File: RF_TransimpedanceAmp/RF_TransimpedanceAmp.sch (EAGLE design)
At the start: 11 parts, among them IC1 OPA847, IC3 PMA-5452, X1 UMC

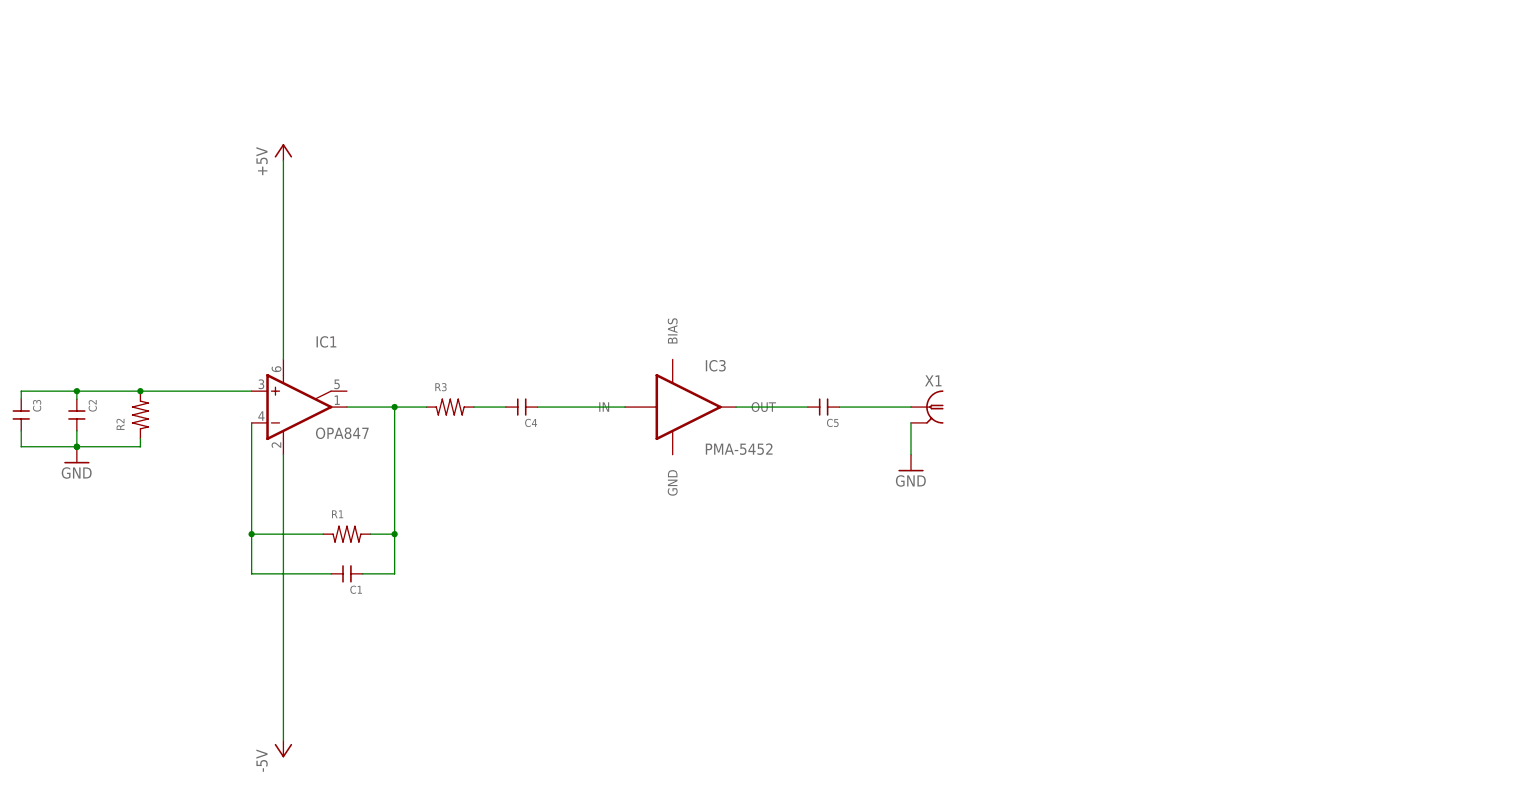
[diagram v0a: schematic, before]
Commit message: Schematic done; routing in progress. Want to check with alessandro.
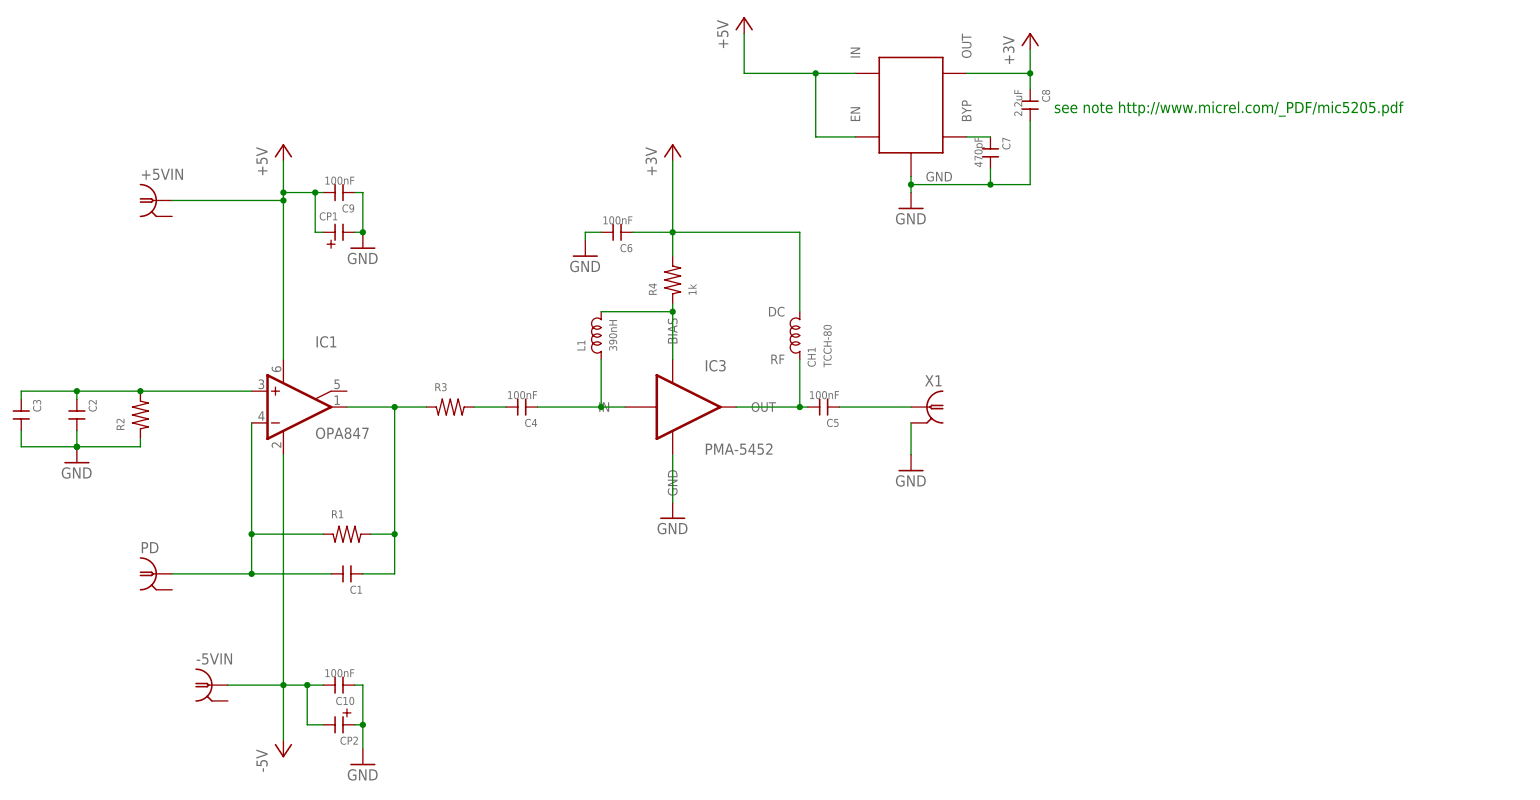
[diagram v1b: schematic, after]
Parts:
- added +5VIN, -5VIN: UMC, connector-jqi:UMC
- added C10, C6, C9: 100nF, rlc-jqi:CAP0201
- added C7: 470pF, rlc-jqi:CAP0201
- added C8: 2.2uF, rlc-jqi:CAP0402
- added CH1: TCCH-80, rf-jqi:TCCH-80
- added CP1, CP2: (no value), rlc-jqi:CAP-POL0603
- added L1: 390nH, rlc-jqi:INDUCTOR-0402
- added PD: SMA, connector-jqi:SMA
- added R4: 1k, rlc-jqi:RES0402
- added U$1: MIC5205, regulator-jqi:MIC5205
- C4, C5: value (none) -> 100nF
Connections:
- new net +3V: C6.P$1, C8.P$1, CH1.DC, R4.P$2, U$1.OUT
- new net N$10: C7.P$1, U$1.BYP
- new net N$9: IC3.BIAS, L1.P$2, R4.P$1
- net +5V: now also +5VIN.1, C9.P$2, CP1.P$1, U$1.EN, U$1.IN
- net -5V: now also -5VIN.1, C10.P$2, CP2.P$2
- net GND: now also C10.P$1, C6.P$2, C7.P$2, C8.P$2, C9.P$1, CP1.P$2, CP2.P$1, IC3.GND, U$1.GND
- net N$2: now also PD.1
- net N$5: now also L1.P$1
- net N$6: now also CH1.RF
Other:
- note added: "see note http://www.micrel.com/_PDF/mic5205.pdf"
